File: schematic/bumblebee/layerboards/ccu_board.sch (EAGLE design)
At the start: 6 parts, among them P1 B4B-EH-A

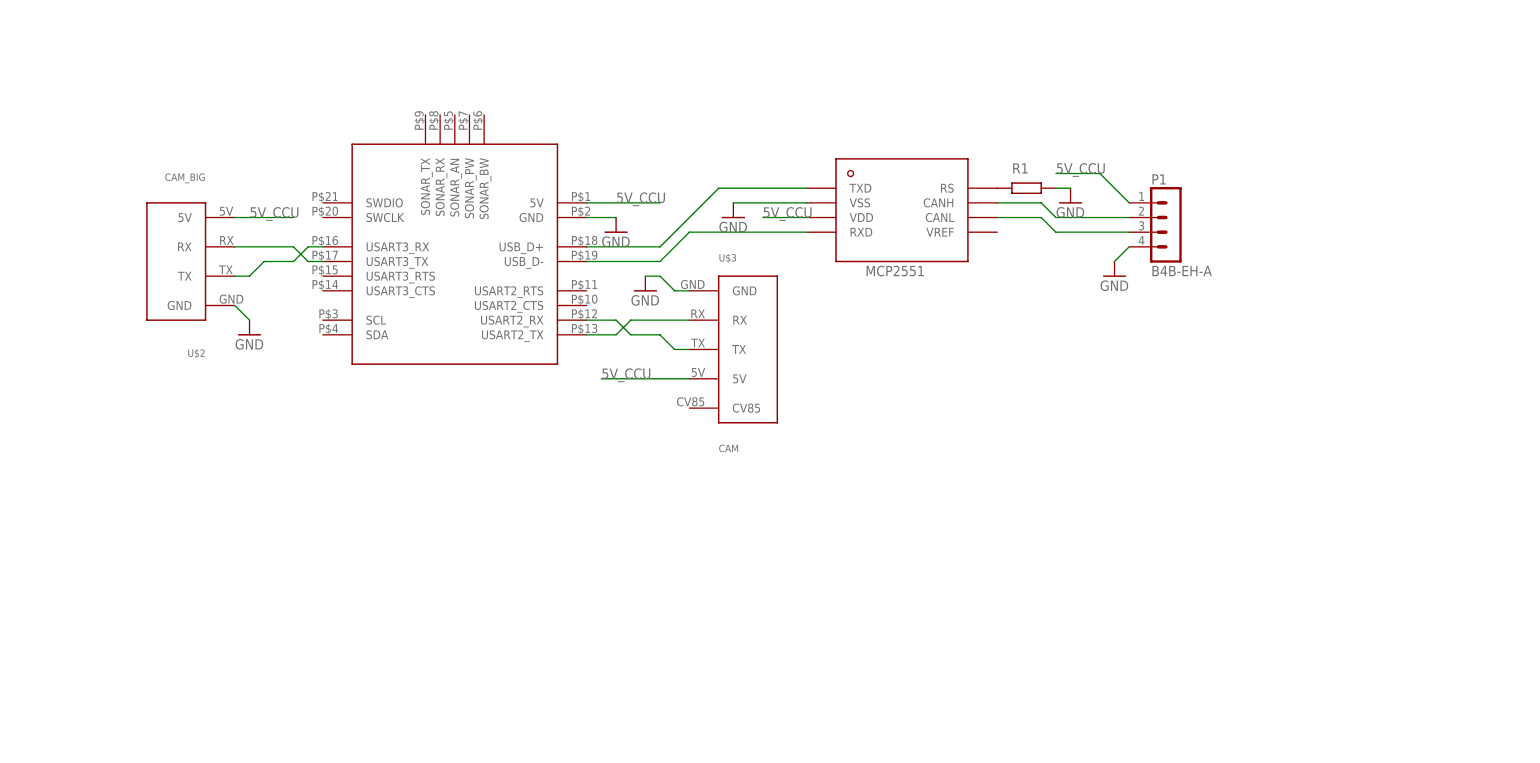
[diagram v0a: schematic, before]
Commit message: Добавил либу SparkFun Идёт работа над CCU и SCU
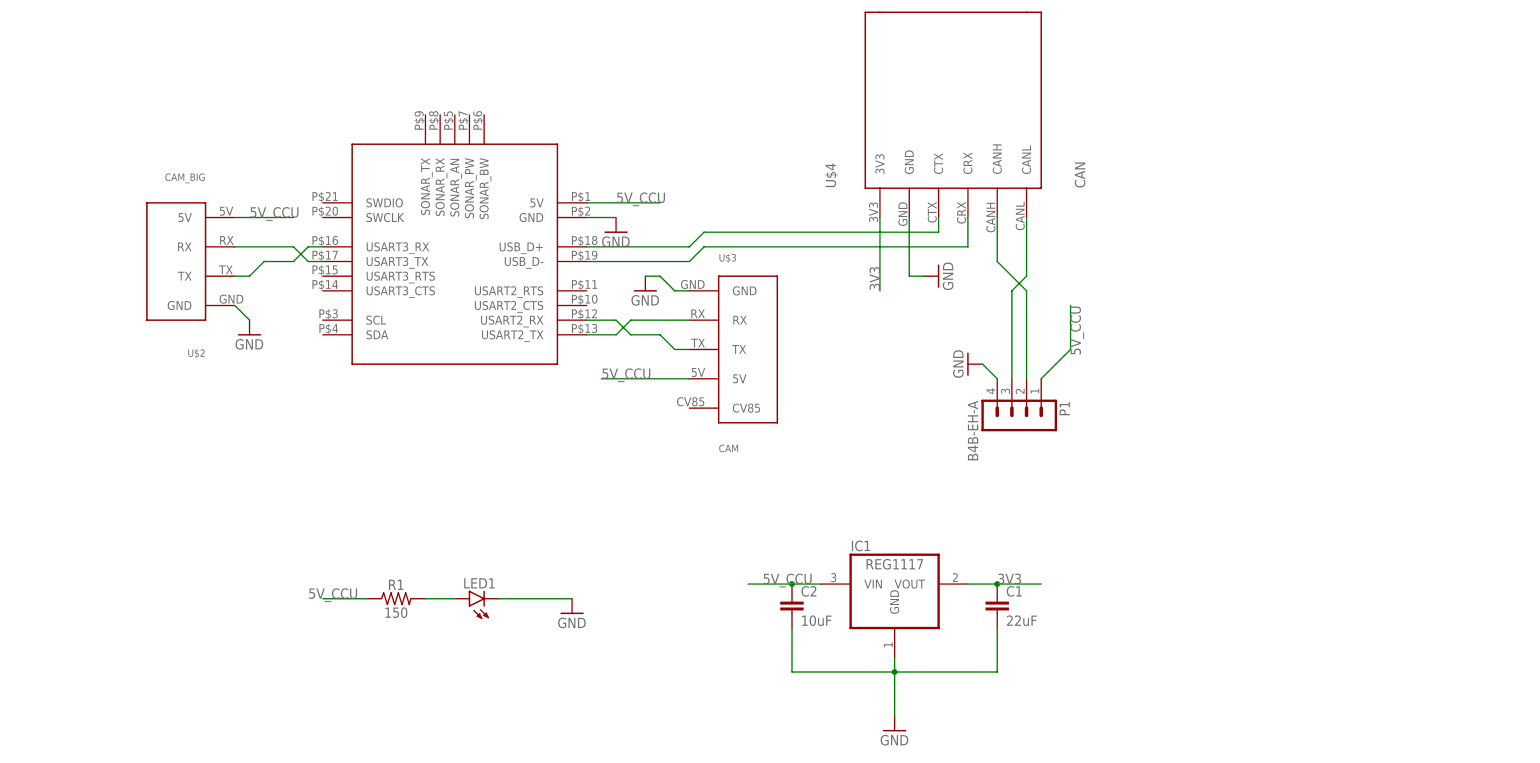
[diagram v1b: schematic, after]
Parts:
- added C1: 22uF, SparkFun-Capacitors:22UF-0805-6.3V-20%
- added C2: 10uF, SparkFun-Capacitors:22UF-0805-16V-20%
- added IC1: REG1117, burr-brown:REG1117
- added LED1: (no value), led:LED5MM
- R1: value (none) -> 150; device ngspice-simulation:R -> SparkFun-Resistors:RESISTORAXIAL-0.3
- U$4: value MCP2551 -> CAN; device MCP2551:MCP2551 -> bluepill:CAN
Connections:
- removed net N$6 (its old number): U$1.USB_D-, U$4.RXD
- new net 3V3: C1.1, IC1.VOUT, U$4.3V3
- new net N$11: LED1.A, R1.2
- net 5V_CCU: now also C2.1, IC1.VIN, R1.1; no longer U$4.VDD
- net GND: now also C1.2, C2.2, IC1.GND, LED1.C, U$4.GND; no longer R1.2, U$4.VSS
- net N$5: now also U$4.CTX; no longer U$4.TXD
- net N$7: now also U$1.USB_D-, U$4.CRX; no longer R1.1, U$4.RS
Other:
- moved on the sheet: P1

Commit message: Ведётся работа по платам. Готовы SCU и CCU
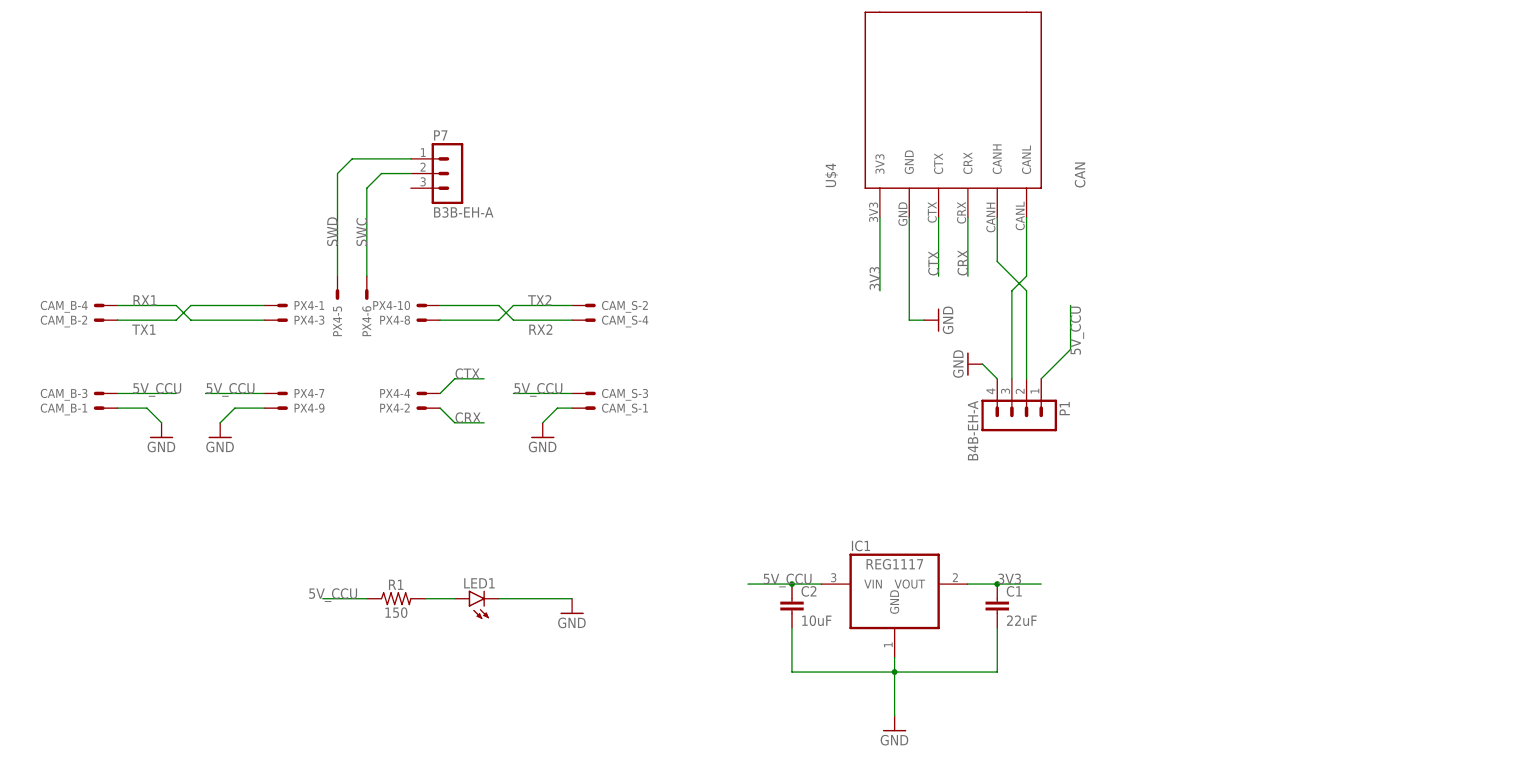
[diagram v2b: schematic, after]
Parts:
- removed U$1: PX4FLOW, bluepill:PX4FLOW
- removed U$2: CAM_BIG, bluepill:CAM_BIG
- removed U$3: CAM, bluepill:CAM
- added CAM_B, CAM_S: 87758-0416, con-molex:87758-0416
- added P7: B3B-EH-A, con-jst-eh:B3B-EH-A
- added PX4: 87758-1016, con-molex:87758-1016
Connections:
- removed net N$1: U$1.USART3_RX, U$2.TX
- removed net N$2: U$1.USART3_TX, U$2.RX
- removed net N$3: U$1.USART2_RX, U$3.TX
- removed net N$4: U$1.USART2_TX, U$3.RX
- removed net N$5: U$1.USB_D+, U$4.CTX
- removed net N$7: U$1.USB_D-, U$4.CRX
- new net CRX: PX4-2.S, U$4.CRX
- new net CTX: PX4-4.S, U$4.CTX
- new net RX1: CAM_B-4.S, PX4-3.S
- new net RX2: CAM_S-4.S, PX4-10.S
- new net SWC: P7.2, PX4-6.S
- new net SWD: P7.1, PX4-5.S
- new net TX1: CAM_B-2.S, PX4-1.S
- new net TX2: CAM_S-2.S, PX4-8.S
- net 5V_CCU: now also CAM_B-3.S, CAM_S-3.S, PX4-7.S; no longer U$1.5V, U$2.5V, U$3.5V
- net GND: now also CAM_B-1.S, CAM_S-1.S, PX4-9.S; no longer U$1.GND, U$2.GND, U$3.GND

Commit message: CCU и ICU полностью готовы. Было бы здорово, если бы ещё кто-то посмотрел По SCU требуются уточнения
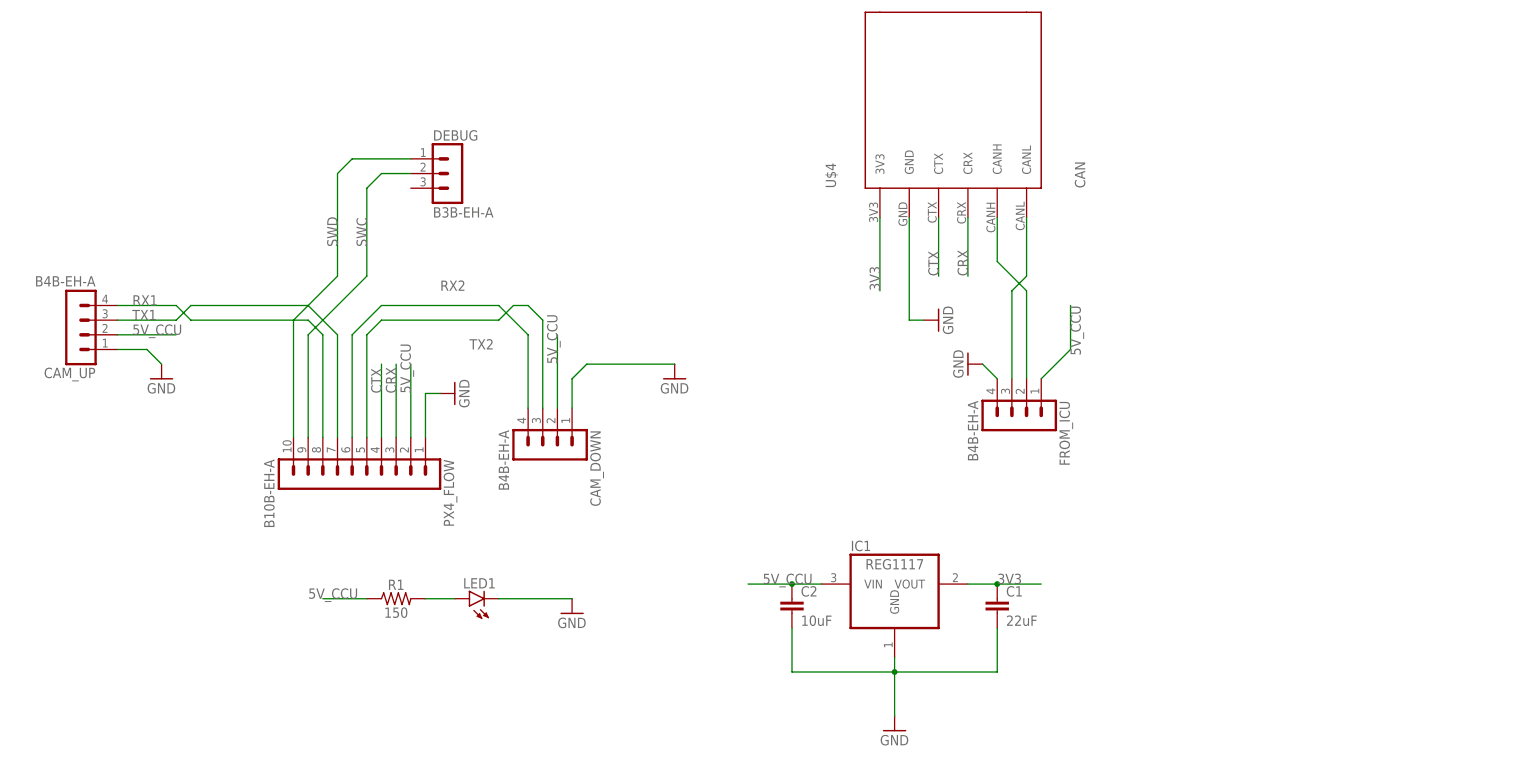
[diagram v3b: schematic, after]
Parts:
- removed CAM_B, CAM_S: 87758-0416, con-molex:87758-0416
- removed PX4: 87758-1016, con-molex:87758-1016
- added CAM_DOWN, CAM_UP: B4B-EH-A, con-jst-eh:B4B-EH-A
- added PX4_FLOW: B10B-EH-A, con-jst-eh:B10B-EH-A
- renumbered P1 to FROM_ICU, P7 to DEBUG
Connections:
- net 5V_CCU: now also CAM_DOWN.2, CAM_UP.2, PX4_FLOW.2; no longer CAM_B-3.S, CAM_S-3.S, PX4-7.S
- net CRX: now also PX4_FLOW.3; no longer PX4-2.S
- net CTX: now also PX4_FLOW.4; no longer PX4-4.S
- net GND: now also CAM_DOWN.1, CAM_UP.1, PX4_FLOW.1; no longer CAM_B-1.S, CAM_S-1.S, PX4-9.S
- net RX1: now also CAM_UP.4, PX4_FLOW.8; no longer CAM_B-4.S, PX4-3.S
- net RX2: now also CAM_DOWN.4, PX4_FLOW.6; no longer CAM_S-4.S, PX4-10.S
- net SWC: now also PX4_FLOW.9; no longer PX4-6.S
- net SWD: now also PX4_FLOW.10; no longer PX4-5.S
- net TX1: now also CAM_UP.3, PX4_FLOW.7; no longer CAM_B-2.S, PX4-1.S
- net TX2: now also CAM_DOWN.3, PX4_FLOW.5; no longer CAM_S-2.S, PX4-8.S

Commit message: Подготовка плат к производству
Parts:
- renumbered IC1 to LDO, U$4 to CAN
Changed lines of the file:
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@@
 <?xml version="1.0" encoding="utf-8"?>
 <!DOCTYPE eagle SYSTEM "eagle.dtd">
-<eagle version="9.3.0">
+<eagle version="9.3.2">
 <drawing>
 <settings>
@@
 <part name="FROM_ICU" library="con-jst-eh" deviceset="B4B-EH-A" device=""/>
 <part name="GND6" library="supply1" library_urn="urn:adsk.eagle:library:371" deviceset="GND" device=""/>
-<part name="U$4" library="bluepill" deviceset="CAN" device=""/>
+<part name="CAN" library="bluepill" deviceset="CAN" device=""/>
 <part name="GND4" library="supply1" library_urn="urn:adsk.eagle:library:371" deviceset="GND" device=""/>
-<part name="IC1" library="burr-brown" library_urn="urn:adsk.eagle:library:111" deviceset="REG1117" device="" package3d_urn="urn:adsk.eagle:package:4940/1"/>
+<part name="LDO" library="burr-brown" library_urn="urn:adsk.eagle:library:111" deviceset="REG1117" device="" package3d_urn="urn:adsk.eagle:package:4940/1"/>
 <part name="GND5" library="supply1" library_urn="urn:adsk.eagle:library:371" deviceset="GND" device=""/>
 <part name="C1" library="SparkFun-Capacitors" deviceset="22UF" device="-0805-6.3V-20%" value="22uF"/>
@@
 <attribute name="VALUE" x="104.14" y="-35.56" size="1.778" layer="96" rot="R270"/>
 </instance>
-<instance part="U$4" gate="G$1" x="104.14" y="7.62" smashed="yes" rot="R90">
+<instance part="CAN" gate="G$1" x="104.14" y="7.62" smashed="yes" rot="R90">
 <attribute name="NAME" x="83.82" y="-7.62" size="1.778" layer="95" rot="R90"/>
 <attribute name="VALUE" x="127" y="-7.62" size="1.778" layer="96" rot="R90"/>
@@
 <attribute name="VALUE" x="104.14" y="-33.02" size="1.778" layer="96" rot="R90"/>
 </instance>
-<instance part="IC1" gate="G$1" x="93.98" y="-76.2" smashed="yes">
+<instance part="LDO" gate="G$1" x="93.98" y="-76.2" smashed="yes">
 <attribute name="NAME" x="86.36" y="-70.485" size="1.778" layer="95" ratio="10"/>
 <attribute name="VALUE" x="88.9" y="-73.66" size="1.778" layer="96" ratio="10"/>
@@
 </segment>
 <segment>
-<pinref part="IC1" gate="G$1" pin="VIN"/>
+<pinref part="LDO" gate="G$1" pin="VIN"/>
 <wire x1="81.28" y1="-76.2" x2="76.2" y2="-76.2" width="0.1524" layer="91"/>
 <label x="71.12" y="-76.2" size="1.778" layer="95"/>
@@
 </segment>
 <segment>
-<pinref part="IC1" gate="G$1" pin="GND"/>
+<pinref part="LDO" gate="G$1" pin="GND"/>
 <pinref part="GND5" gate="1" pin="GND"/>
 <wire x1="93.98" y1="-99.06" x2="93.98" y2="-91.44" width="0.1524" layer="91"/>
@@
 </segment>
 <segment>
-<pinref part="U$4" gate="G$1" pin="GND"/>
+<pinref part="CAN" gate="G$1" pin="GND"/>
 <wire x1="96.52" y1="-12.7" x2="96.52" y2="-30.48" width="0.1524" layer="91"/>
 <wire x1="96.52" y1="-30.48" x2="99.06" y2="-30.48" width="0.1524" layer="91"/>
@@
 <net name="N$6" class="0">
 <segment>
-<pinref part="U$4" gate="G$1" pin="CANL"/>
+<pinref part="CAN" gate="G$1" pin="CANL"/>
 <wire x1="116.84" y1="-12.7" x2="116.84" y2="-22.86" width="0.1524" layer="91"/>
 <wire x1="116.84" y1="-22.86" x2="114.3" y2="-25.4" width="0.1524" layer="91"/>
@@
 <net name="N$8" class="0">
 <segment>
-<pinref part="U$4" gate="G$1" pin="CANH"/>
+<pinref part="CAN" gate="G$1" pin="CANH"/>
 <wire x1="111.76" y1="-12.7" x2="111.76" y2="-20.32" width="0.1524" layer="91"/>
 <wire x1="111.76" y1="-20.32" x2="116.84" y2="-25.4" width="0.1524" layer="91"/>
@@
 <net name="3V3" class="0">
 <segment>
-<pinref part="U$4" gate="G$1" pin="3V3"/>
+<pinref part="CAN" gate="G$1" pin="3V3"/>
 <wire x1="91.44" y1="-12.7" x2="91.44" y2="-25.4" width="0.1524" layer="91"/>
 <label x="91.44" y="-25.4" size="1.778" layer="95" rot="R90"/>
 </segment>
 <segment>
-<pinref part="IC1" gate="G$1" pin="VOUT"/>
+<pinref part="LDO" gate="G$1" pin="VOUT"/>
 <wire x1="106.68" y1="-76.2" x2="111.76" y2="-76.2" width="0.1524" layer="91"/>
 <label x="111.76" y="-76.2" size="1.778" layer="95"/>
@@
 <net name="CRX" class="0">
 <segment>
-<pinref part="U$4" gate="G$1" pin="CRX"/>
+<pinref part="CAN" gate="G$1" pin="CRX"/>
 <wire x1="106.68" y1="-12.7" x2="106.68" y2="-22.86" width="0.1524" layer="91"/>
 <label x="106.68" y="-22.86" size="1.778" layer="95" rot="R90"/>
@@
 <net name="CTX" class="0">
 <segment>
-<pinref part="U$4" gate="G$1" pin="CTX"/>
+<pinref part="CAN" gate="G$1" pin="CTX"/>
 <wire x1="101.6" y1="-12.7" x2="101.6" y2="-22.86" width="0.1524" layer="91"/>
 <label x="101.6" y="-22.86" size="1.778" layer="95" rot="R90"/>
@@
 </sheet>
 </sheets>
+<errors>
+</errors>
 </schematic>
 </drawing>
